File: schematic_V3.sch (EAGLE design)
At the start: 20 parts, among them IC1 VR1, J1 POWER_JACKPTH

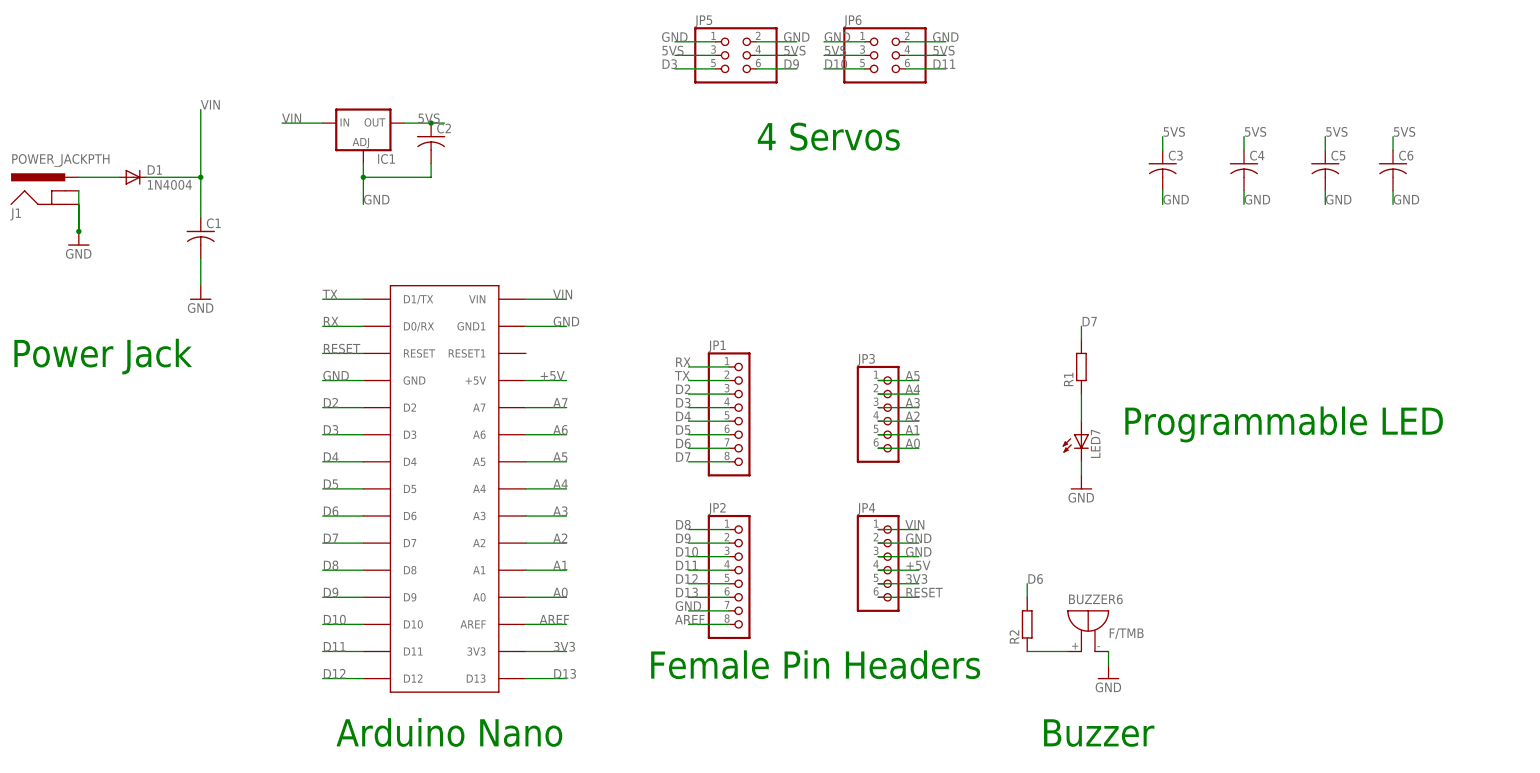
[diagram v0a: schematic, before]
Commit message: Add files via upload
Connected 5VS and +5V rails. Minor cleanup of warnings prompted in Eagle
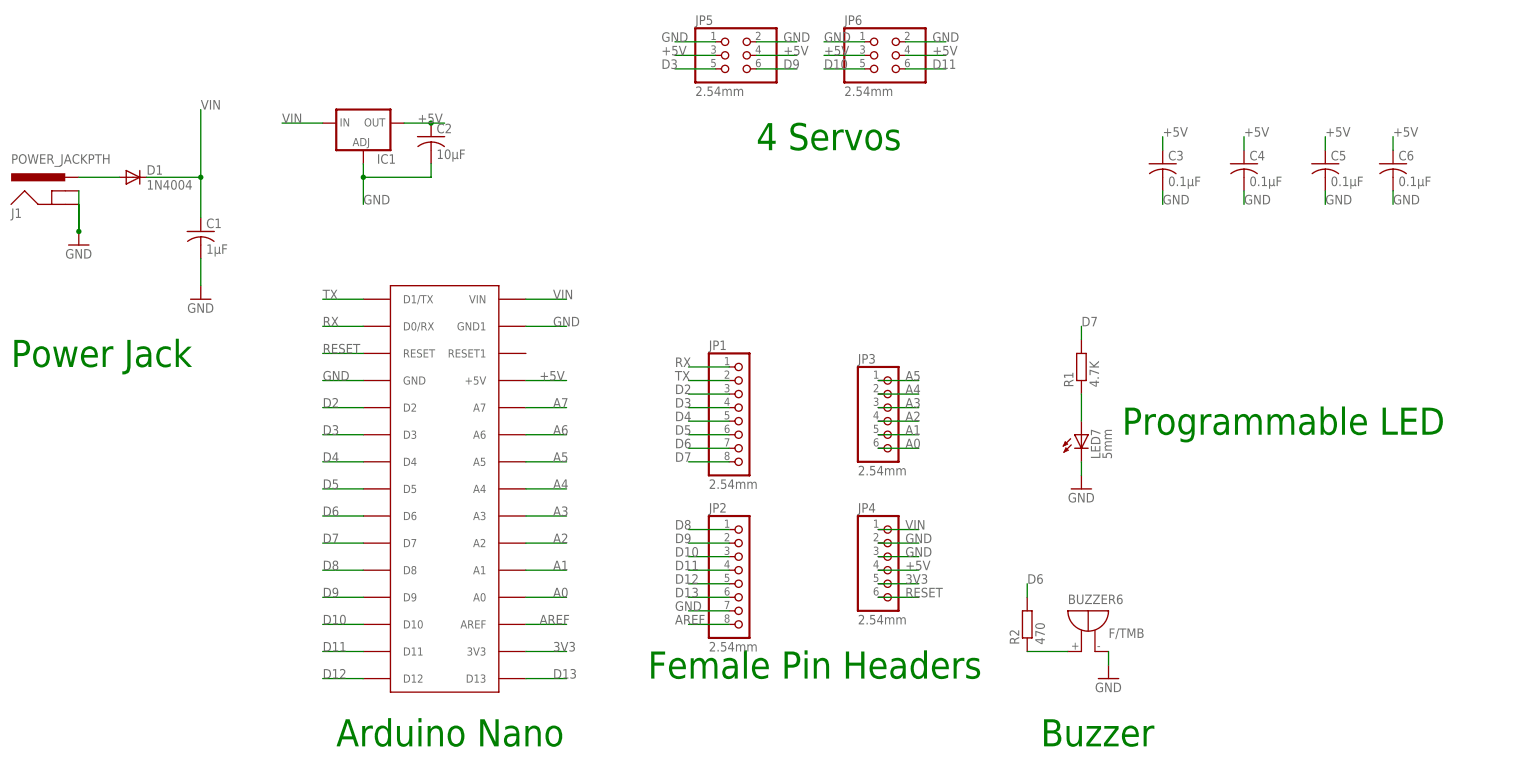
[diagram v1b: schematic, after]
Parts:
- C1: value (none) -> 1μF
- C2: value (none) -> 10μF
- C3, C4, C5, C6: value (none) -> 0.1μF
- JP1, JP2, JP3, JP4, JP5, JP6: value (none) -> 2.54mm
- LED7: value (none) -> 5mm
- R1: value (none) -> 4.7K
- R2: value (none) -> 470
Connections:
- removed net 5VS: C2.1, C3.1, C4.1, C5.1, C6.1, IC1.OUT, JP5.3, JP5.4, JP6.3, JP6.4
- net +5V: now also C2.1, C3.1, C4.1, C5.1, C6.1, IC1.OUT, JP5.3, JP5.4, JP6.3, JP6.4
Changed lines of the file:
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@@
 <?xml version="1.0" encoding="utf-8"?>
 <!DOCTYPE eagle SYSTEM "eagle.dtd">
-<eagle version="7.5.0">
+<eagle version="9.0.1">
 <drawing>
 <settings>
 <setting alwaysvectorfont="no"/>
+<setting keepoldvectorfont="yes"/>
 <setting verticaltext="up"/>
 </settings>
@@
 <parts>
 <part name="U$1" library="rocketfarm" deviceset="ARDUINONANO" device=""/>
-<part name="JP1" library="pinhead" deviceset="PINHD-1X8" device=""/>
-<part name="JP2" library="pinhead" deviceset="PINHD-1X8" device=""/>
-<part name="JP3" library="pinhead" deviceset="PINHD-1X6" device=""/>
-<part name="JP4" library="pinhead" deviceset="PINHD-1X6" device=""/>
-<part name="R1" library="rcl" deviceset="R-EU_" device="0207/10"/>
-<part name="R2" library="rcl" deviceset="R-EU_" device="0207/10"/>
-<part name="LED7" library="led" deviceset="LED" device="5MM"/>
+<part name="JP1" library="pinhead" deviceset="PINHD-1X8" device="" value="2.54mm"/>
+<part name="JP2" library="pinhead" deviceset="PINHD-1X8" device="" value="2.54mm"/>
+<part name="JP3" library="pinhead" deviceset="PINHD-1X6" device="" value="2.54mm"/>
+<part name="JP4" library="pinhead" deviceset="PINHD-1X6" device="" value="2.54mm"/>
+<part name="R1" library="rcl" deviceset="R-EU_" device="0207/10" value="4.7K"/>
+<part name="R2" library="rcl" deviceset="R-EU_" device="0207/10" value="470"/>
+<part name="LED7" library="led" deviceset="LED" device="5MM" value="5mm"/>
 <part name="BUZZER6" library="buzzer" deviceset="F/TMB" device=""/>
 <part name="GND1" library="supply1" deviceset="GND" device=""/>
@@
 <part name="J1" library="SparkFun" deviceset="POWER_JACK" device="PTH"/>
 <part name="D1" library="diode" deviceset="1N4004" device=""/>
-<part name="C1" library="adafruit" deviceset="C-US" device="C1206"/>
+<part name="C1" library="adafruit" deviceset="C-US" device="C1206" value="1μF"/>
 <part name="GND3" library="supply1" deviceset="GND" device=""/>
 <part name="GND4" library="supply1" deviceset="GND" device=""/>
 <part name="IC1" library="v-reg" deviceset="LD117A?*" device="S" technology="33TR" value="VR1"/>
-<part name="C2" library="adafruit" deviceset="C-US" device="C1206"/>
-<part name="C3" library="adafruit" deviceset="C-US" device="C1206"/>
-<part name="C4" library="adafruit" deviceset="C-US" device="C1206"/>
-<part name="C5" library="adafruit" deviceset="C-US" device="C1206"/>
-<part name="C6" library="adafruit" deviceset="C-US" device="C1206"/>
-<part name="JP5" library="pinhead" deviceset="PINHD-2X3" device=""/>
-<part name="JP6" library="pinhead" deviceset="PINHD-2X3" device=""/>
+<part name="C2" library="adafruit" deviceset="C-US" device="C1206" value="10μF"/>
+<part name="C3" library="adafruit" deviceset="C-US" device="C1206" value="0.1μF"/>
+<part name="C4" library="adafruit" deviceset="C-US" device="C1206" value="0.1μF"/>
+<part name="C5" library="adafruit" deviceset="C-US" device="C1206" value="0.1μF"/>
+<part name="C6" library="adafruit" deviceset="C-US" device="C1206" value="0.1μF"/>
+<part name="JP5" library="pinhead" deviceset="PINHD-2X3" device="" value="2.54mm"/>
+<part name="JP6" library="pinhead" deviceset="PINHD-2X3" device="" value="2.54mm"/>
 </parts>
 <sheets>
@@
 <label x="88.9" y="53.34" size="1.778" layer="95"/>
 </segment>
-</net>
-<net name="3V3" class="0">
-<segment>
-<pinref part="JP4" gate="A" pin="5"/>
-<wire x1="152.4" y1="15.24" x2="160.02" y2="15.24" width="0.1524" layer="91"/>
-<label x="157.48" y="15.24" size="1.778" layer="95"/>
-</segment>
-<segment>
-<pinref part="U$1" gate="G$1" pin="3V3"/>
-<wire x1="86.36" y1="2.54" x2="93.98" y2="2.54" width="0.1524" layer="91"/>
-<label x="91.44" y="2.54" size="1.778" layer="95"/>
-</segment>
-</net>
-<net name="RESET" class="0">
-<segment>
-<pinref part="U$1" gate="G$1" pin="RESET"/>
-<wire x1="55.88" y1="58.42" x2="48.26" y2="58.42" width="0.1524" layer="91"/>
-<label x="48.26" y="58.42" size="1.778" layer="95"/>
-</segment>
-<segment>
-<pinref part="JP4" gate="A" pin="6"/>
-<wire x1="152.4" y1="12.7" x2="160.02" y2="12.7" width="0.1524" layer="91"/>
-<label x="157.48" y="12.7" size="1.778" layer="95"/>
-</segment>
-</net>
-<net name="A6" class="0">
-<segment>
-<pinref part="U$1" gate="G$1" pin="A6"/>
-<wire x1="86.36" y1="43.18" x2="93.98" y2="43.18" width="0.1524" layer="91"/>
-<label x="91.44" y="43.18" size="1.778" layer="95"/>
-</segment>
-</net>
-<net name="A7" class="0">
-<segment>
-<pinref part="U$1" gate="G$1" pin="A7"/>
-<wire x1="86.36" y1="48.26" x2="93.98" y2="48.26" width="0.1524" layer="91"/>
-<label x="91.44" y="48.26" size="1.778" layer="95"/>
-</segment>
-</net>
-<net name="N$1" class="0">
-<segment>
-<pinref part="R1" gate="G$1" pin="1"/>
-<pinref part="LED7" gate="G$1" pin="A"/>
-<wire x1="190.5" y1="45.72" x2="190.5" y2="50.8" width="0.1524" layer="91"/>
-</segment>
-</net>
-<net name="N$4" class="0">
-<segment>
-<pinref part="R2" gate="G$1" pin="1"/>
-<pinref part="BUZZER6" gate="1" pin="+"/>
-<wire x1="180.34" y1="2.54" x2="187.96" y2="2.54" width="0.1524" layer="91"/>
-</segment>
-</net>
-<net name="N$2" class="0">
-<segment>
-<pinref part="J1" gate="G$1" pin="PWR"/>
-<pinref part="D1" gate="1" pin="A"/>
-<wire x1="2.54" y1="91.44" x2="10.16" y2="91.44" width="0.1524" layer="91"/>
-</segment>
-</net>
-<net name="5VS" class="0">
 <segment>
 <pinref part="IC1" gate="G$1" pin="OUT"/>
@@
 </segment>
 <segment>
+<pinref part="JP5" gate="A" pin="3"/>
+<wire x1="121.92" y1="114.3" x2="114.3" y2="114.3" width="0.1524" layer="91"/>
+<label x="111.76" y="114.3" size="1.778" layer="95"/>
+</segment>
+<segment>
+<pinref part="JP5" gate="A" pin="4"/>
+<wire x1="129.54" y1="114.3" x2="137.16" y2="114.3" width="0.1524" layer="91"/>
+<label x="134.62" y="114.3" size="1.778" layer="95"/>
+</segment>
+<segment>
+<pinref part="JP6" gate="A" pin="3"/>
+<wire x1="149.86" y1="114.3" x2="142.24" y2="114.3" width="0.1524" layer="91"/>
+<label x="142.24" y="114.3" size="1.778" layer="95"/>
+</segment>
+<segment>
+<pinref part="JP6" gate="A" pin="4"/>
+<wire x1="157.48" y1="114.3" x2="165.1" y2="114.3" width="0.1524" layer="91"/>
+<label x="162.56" y="114.3" size="1.778" layer="95"/>
+</segment>
+<segment>
 <pinref part="C3" gate="G$1" pin="1"/>
 <wire x1="205.74" y1="96.52" x2="205.74" y2="99.06" width="0.1524" layer="91"/>
@@
 <label x="248.92" y="99.06" size="1.778" layer="95"/>
 </segment>
-<segment>
-<pinref part="JP5" gate="A" pin="3"/>
-<wire x1="121.92" y1="114.3" x2="114.3" y2="114.3" width="0.1524" layer="91"/>
-<label x="111.76" y="114.3" size="1.778" layer="95"/>
-</segment>
-<segment>
-<pinref part="JP5" gate="A" pin="4"/>
-<wire x1="129.54" y1="114.3" x2="137.16" y2="114.3" width="0.1524" layer="91"/>
-<label x="134.62" y="114.3" size="1.778" layer="95"/>
-</segment>
-<segment>
-<pinref part="JP6" gate="A" pin="3"/>
-<wire x1="149.86" y1="114.3" x2="142.24" y2="114.3" width="0.1524" layer="91"/>
-<label x="142.24" y="114.3" size="1.778" layer="95"/>
-</segment>
-<segment>
-<pinref part="JP6" gate="A" pin="4"/>
-<wire x1="157.48" y1="114.3" x2="165.1" y2="114.3" width="0.1524" layer="91"/>
-<label x="162.56" y="114.3" size="1.778" layer="95"/>
+</net>
+<net name="3V3" class="0">
+<segment>
+<pinref part="JP4" gate="A" pin="5"/>
+<wire x1="152.4" y1="15.24" x2="160.02" y2="15.24" width="0.1524" layer="91"/>
+<label x="157.48" y="15.24" size="1.778" layer="95"/>
+</segment>
+<segment>
+<pinref part="U$1" gate="G$1" pin="3V3"/>
+<wire x1="86.36" y1="2.54" x2="93.98" y2="2.54" width="0.1524" layer="91"/>
+<label x="91.44" y="2.54" size="1.778" layer="95"/>
+</segment>
+</net>
+<net name="RESET" class="0">
+<segment>
+<pinref part="U$1" gate="G$1" pin="RESET"/>
+<wire x1="55.88" y1="58.42" x2="48.26" y2="58.42" width="0.1524" layer="91"/>
+<label x="48.26" y="58.42" size="1.778" layer="95"/>
+</segment>
+<segment>
+<pinref part="JP4" gate="A" pin="6"/>
+<wire x1="152.4" y1="12.7" x2="160.02" y2="12.7" width="0.1524" layer="91"/>
+<label x="157.48" y="12.7" size="1.778" layer="95"/>
+</segment>
+</net>
+<net name="A6" class="0">
+<segment>
+<pinref part="U$1" gate="G$1" pin="A6"/>
+<wire x1="86.36" y1="43.18" x2="93.98" y2="43.18" width="0.1524" layer="91"/>
+<label x="91.44" y="43.18" size="1.778" layer="95"/>
+</segment>
+</net>
+<net name="A7" class="0">
+<segment>
+<pinref part="U$1" gate="G$1" pin="A7"/>
+<wire x1="86.36" y1="48.26" x2="93.98" y2="48.26" width="0.1524" layer="91"/>
+<label x="91.44" y="48.26" size="1.778" layer="95"/>
+</segment>
+</net>
+<net name="N$1" class="0">
+<segment>
+<pinref part="R1" gate="G$1" pin="1"/>
+<pinref part="LED7" gate="G$1" pin="A"/>
+<wire x1="190.5" y1="45.72" x2="190.5" y2="50.8" width="0.1524" layer="91"/>
+</segment>
+</net>
+<net name="N$4" class="0">
+<segment>
+<pinref part="R2" gate="G$1" pin="1"/>
+<pinref part="BUZZER6" gate="1" pin="+"/>
+<wire x1="180.34" y1="2.54" x2="187.96" y2="2.54" width="0.1524" layer="91"/>
+</segment>
+</net>
+<net name="N$2" class="0">
+<segment>
+<pinref part="J1" gate="G$1" pin="PWR"/>
+<pinref part="D1" gate="1" pin="A"/>
+<wire x1="2.54" y1="91.44" x2="10.16" y2="91.44" width="0.1524" layer="91"/>
 </segment>
 </net>
@@
 </sheet>
 </sheets>
+<errors>
+</errors>
 </schematic>
 </drawing>
